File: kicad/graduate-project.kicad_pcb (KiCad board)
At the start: 2 copper layers, 43.2 x 76.2 mm, 16 parts, among them J1 Power, J2 GY-9250, J3 HM-10, J4 Left Motor, J5 Right Motor, U1 NUCLEO-L432KC, U2 DRV8847PWP

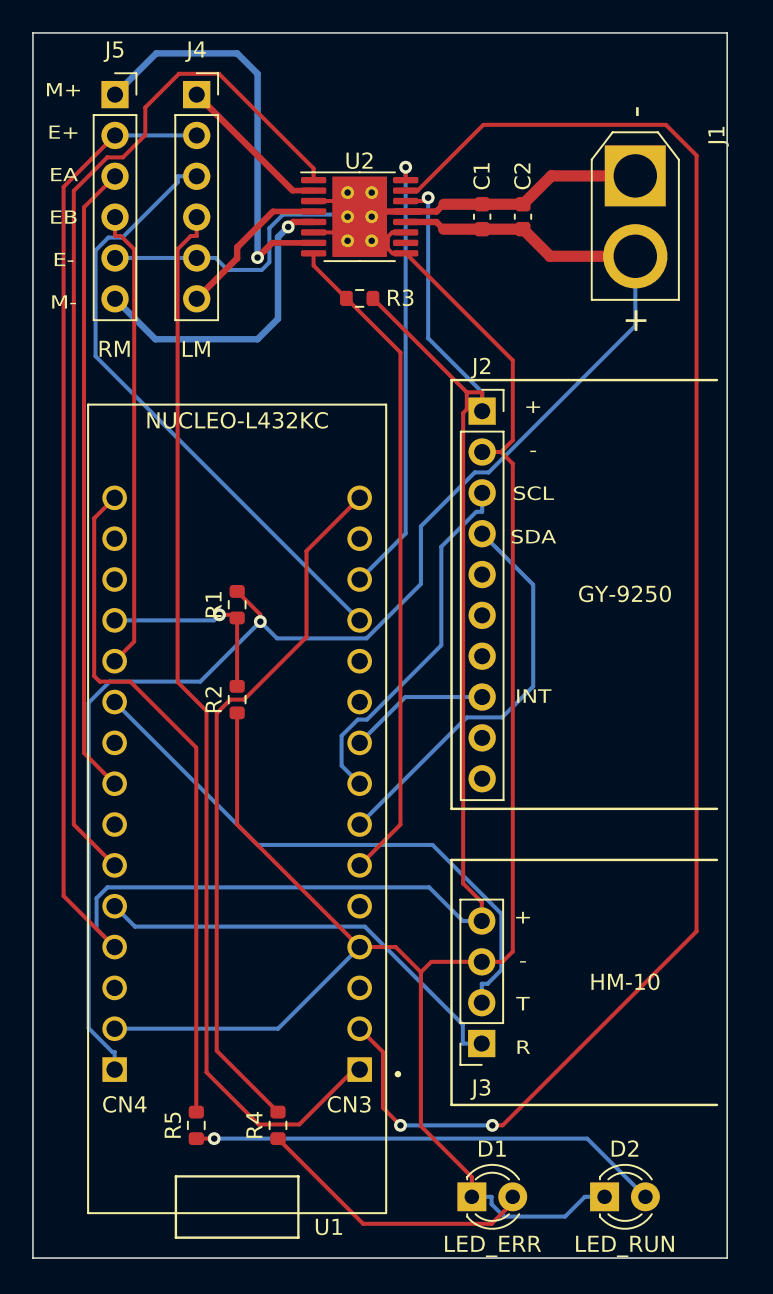
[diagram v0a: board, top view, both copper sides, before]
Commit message: Change DRV8824 interface mode from 2-Pin to 4-Pin
* MOD: Drop ENC_2A, B (use only left motor encoder)
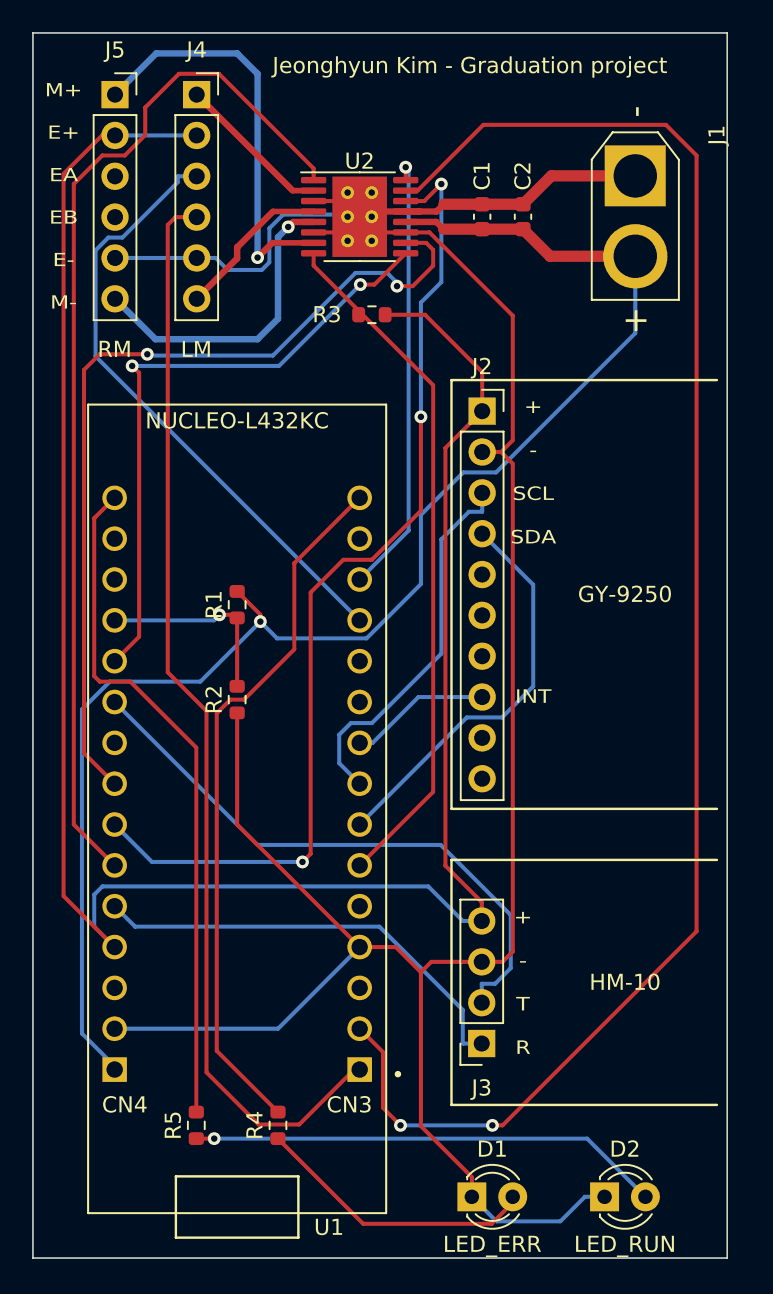
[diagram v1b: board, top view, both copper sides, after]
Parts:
- moved R3 1.27 mm to (71.9, 55.6)
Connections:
- J5 pad 3: ENC_2A -> unconnected-(J5-Pad3)
- J5 pad 4: ENC_2B -> unconnected-(J5-Pad4)
- U1 pad CN4_11: ENC_2B -> M_IN3
- U1 pad CN4_7: unconnected-(U1-PadCN4_7) -> M_MODE
- U1 pad CN4_8: ENC_2A -> M_IN4
- U2 pad 10: unconnected-(U2-Pad10) -> M_IN4
- U2 pad 14: ENC_VCC -> M_MODE
- U2 pad 9: BATT_GND -> M_IN3
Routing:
- net M_MODE: track 0.00 -> 62.1 mm, vias 0 -> 3
- net M_IN4: track 0.00 -> 54.7 mm, vias 0 -> 2
- net ENC_2A: track 39.4 -> 0.00 mm
- net M_IN3: track 0.00 -> 39.1 mm, vias 0 -> 2
- net ENC_2B: track 28.8 -> 0.00 mm
- net ENC_VCC: track 146.8 -> 131.0 mm, vias 1 -> 0
- net M_FAULT: track 41.4 -> 43.0 mm
- net BATT_GND: track 170.6 -> 172.1 mm
- net ENC_1B: track 66.9 -> 68.0 mm
- net HM_TX: track 35.8 -> 36.8 mm
- net BATT_VIN: track 92.2 -> 93.2 mm
- net GY_SCL: track 22.7 -> 23.5 mm
- net HM_RX: track 27.1 -> 27.6 mm
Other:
- board text added: "Jeonghyun Kim - Graduation project"

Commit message: Update pdf plots
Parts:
- removed R3: 10k, Resistor_SMD:R_0603_1608Metric
- added ?: , , F.Cu at (72.1, 55.9)
- added ?: , , F.Cu at (72.1, 42.4)
- added ?: , , F.Cu at (73.2, 55.9)
- added ?: , , F.Cu at (72.1, 56.9)
- added ?: , , F.Cu at (73.2, 56.9)
- added ?: , , F.Cu at (72.1, 44.5)
- added ?: , , F.Cu at (73.2, 44.5)
- added ?: , , F.Cu at (72.1, 43.4)
- added ?: , , F.Cu at (73.2, 42.4)
- added ?: , , F.Cu at (72.1, 54.9)
- added ?: , , F.Cu at (73.2, 54.9)
- added ?: , , F.Cu at (73.2, 43.4)
- added C3: 22n, Capacitor_SMD:C_0603_1608Metric, F.Cu at (81.0, 54.4)
- added C4: 100n, Capacitor_SMD:C_0603_1608Metric, F.Cu at (81.0, 57.4)
- added C5: 10u, Capacitor_SMD:C_0603_1608Metric, F.Cu at (83.8, 49.5)
- added C6: 0.1u, Capacitor_SMD:C_0603_1608Metric, F.Cu at (81.0, 49.5)
- added U3: DRV8874PWPR, DRV8874PWPR:SOP65P640X120-17N, F.Cu at (72.6, 43.4)
- C1: value 10u -> 22n
- C2: value 0.1u -> 100n
- U2: value DRV8847PWP -> DRV8874PWPR; footprint Package_SO:HTSSOP-16-1EP_4.4x5mm_P0.65mm_EP3.4x5mm_Mask2.46x2.31mm_ThermalVias -> DRV8874PWPR:SOP65P640X120-17N
- moved C1 7.96 mm to (81.0, 41.9)
- moved U2 6.53 mm to (72.6, 55.9)
- moved C2 4.58 mm to (81.0, 45.0), turned to -90 degrees
- moved J5 2.62 mm to (53.6, 43.2)
- moved J2 2.41 mm to (78.8, 64.0)
- moved U1 2.29 mm to (63.5, 88.6)
- moved J4 1.80 mm to (62.3, 43.2)
- moved J3 1.41 mm to (78.7, 102.4)
- moved J1 1.16 mm to (89.4, 46.8)
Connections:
- C1 pad 1: BATT_VIN -> Net-(C1-Pad1)
- C1 pad 2: BATT_GND -> Net-(C1-Pad2)
- C2 pad 1: BATT_VIN -> Net-(C2-Pad1)
- C2 pad 2: BATT_GND -> BATT_VIN
- J4 pad 1: Net-(J4-Pad1) -> Net-(U2-Pad8)
- J4 pad 6: Net-(J4-Pad6) -> Net-(U2-Pad10)
- U1 pad CN3_6: M_FAULT -> M_FAULT1
- U1 pad CN4_14: unconnected-(U1-PadCN4_14) -> 3_3V
- U1 pad CN4_7: M_MODE -> M_FAULT2
- U2 pad 1: M_OFF -> M_IN3
- U2 pad 10: M_IN4 -> Net-(U2-Pad10)
- U2 pad 11: BATT_GND -> BATT_VIN
- U2 pad 12: BATT_VIN -> Net-(C4-Pad1)
- U2 pad 13: BATT_GND -> Net-(C3-Pad1)
- U2 pad 14: M_MODE -> Net-(C3-Pad2)
- U2 pad 15: M_IN2 -> BATT_GND
- U2 pad 16: M_IN1 -> ENC_VCC
- U2 pad 2: Net-(J4-Pad1) -> M_IN4
- U2 pad 3: BATT_GND -> M_OFF
- U2 pad 4: Net-(J4-Pad6) -> M_FAULT2
- U2 pad 5: Net-(J5-Pad6) -> 3_3V
- U2 pad 7: Net-(J5-Pad1) -> BATT_GND
- U2 pad 8: M_FAULT -> Net-(U2-Pad8)
- U2 pad 9: M_IN3 -> BATT_GND
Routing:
- net M_MODE: track 62.1 -> 0.00 mm, vias 3 -> 0
- net M_FAULT1: track 0.00 -> 61.4 mm
- net M_FAULT2: track 0.00 -> 43.9 mm, vias 0 -> 1
- net M_FAULT: track 43.0 -> 0.00 mm
- net 3_3V: track 0.00 -> 37.8 mm, vias 0 -> 1
- net BATT_GND: track 172.1 -> 203.1 mm
- net M_IN2: track 99.3 -> 73.3 mm, vias 2 -> 0
- net Net-(U2-Pad10): track 0.00 -> 25.1 mm, vias 0 -> 1
- net Net-(U2-Pad8): track 0.00 -> 22.8 mm, vias 0 -> 1
- net BATT_VIN: track 93.2 -> 110.7 mm, vias 1 -> 2
- net ENC_1A: track 38.2 -> 51.9 mm
- net ENC_VCC: track 131.0 -> 117.3 mm, vias 0 -> 1
- net Net-(J5-Pad6): track 19.4 -> 32.3 mm
- net LED_ERR: track 44.0 -> 56.0 mm
- net M_IN4: track 54.7 -> 42.9 mm, vias 2 -> 1
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- added copper zone on B.Cu, net BATT_GND
- added copper zone on F.Cu, net BATT_GND
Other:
- board text added: "Jeonghyun Kim"
- board text removed: "Jeonghyun Kim - Graduation project"
